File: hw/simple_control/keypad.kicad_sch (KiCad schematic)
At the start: 2 parts, among them U1501 4050

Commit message: chore(hw): add buttons layout
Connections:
- net Filtered Button 4/SW is gone; now on net GND: U1501.11
- net Filtered Button 5/SW is gone; now on net GND: U1501.14
- net BTN4: no longer names the net of U1501.12
- net BTN5: no longer names the net of U1501.15
- no-connect marks 0 -> 2
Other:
- removed sheet Filtered Button 4
- removed sheet Filtered Button 5
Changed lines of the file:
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@@
   (junction (at 204.47 86.36) (diameter 0) (color 0 0 0 0)
   )
+  (no_connect (at 158.75 128.27))
+  (no_connect (at 158.75 116.84))
   (wire (pts (xy 191.77 86.36) (xy 204.47 86.36))
     (stroke (width 0) (type default))
@@
     (stroke (width 0) (type default))
   )
+  (wire (pts (xy 139.7 128.27) (xy 139.7 129.54))
+    (stroke (width 0) (type default))
+  )
   (wire (pts (xy 204.47 86.36) (xy 204.47 90.17))
     (stroke (width 0) (type default))
@@
     (stroke (width 0) (type default))
   )
-  (wire (pts (xy 158.75 128.27) (xy 161.29 128.27))
+  (wire (pts (xy 139.7 116.84) (xy 139.7 118.11))
     (stroke (width 0) (type default))
   )
@@
     (stroke (width 0) (type default))
   )
-  (wire (pts (xy 158.75 116.84) (xy 161.29 116.84))
-    (stroke (width 0) (type default))
-  )
   (wire (pts (xy 204.47 83.82) (xy 204.47 86.36))
     (stroke (width 0) (type default))
@@
     (stroke (width 0) (type default))
   )
-  (global_label "BTN0" (shape output) (at 161.29 69.85 0) (fields_autoplaced)
+  (hierarchical_label "BTN3" (shape output) (at 161.29 105.41 0) (fields_autoplaced)
     (effects (font (size 1.27 1.27)) (justify left))
-    (property "Intersheetrefs" "${INTERSHEET_REFS}" (at 169.0528 69.85 0)
-      (effects (font (size 1.27 1.27)) (justify left) hide)
-    )
-  )
-  (global_label "BTN3" (shape output) (at 161.29 105.41 0) (fields_autoplaced)
+  )
+  (hierarchical_label "BTN1" (shape output) (at 161.29 82.55 0) (fields_autoplaced)
     (effects (font (size 1.27 1.27)) (justify left))
-    (property "Intersheetrefs" "${INTERSHEET_REFS}" (at 169.0528 105.41 0)
-      (effects (font (size 1.27 1.27)) (justify left) hide)
-    )
-  )
-  (global_label "BTN2" (shape output) (at 161.29 93.98 0) (fields_autoplaced)
+  )
+  (hierarchical_label "BTN2" (shape output) (at 161.29 93.98 0) (fields_autoplaced)
     (effects (font (size 1.27 1.27)) (justify left))
-    (property "Intersheetrefs" "${INTERSHEET_REFS}" (at 169.0528 93.98 0)
-      (effects (font (size 1.27 1.27)) (justify left) hide)
-    )
-  )
-  (global_label "BTN4" (shape output) (at 161.29 116.84 0) (fields_autoplaced)
+  )
+  (hierarchical_label "BTN0" (shape output) (at 161.29 69.85 0) (fields_autoplaced)
     (effects (font (size 1.27 1.27)) (justify left))
-    (property "Intersheetrefs" "${INTERSHEET_REFS}" (at 169.0528 116.84 0)
-      (effects (font (size 1.27 1.27)) (justify left) hide)
-    )
-  )
-  (global_label "BTN1" (shape output) (at 161.29 82.55 0) (fields_autoplaced)
-    (effects (font (size 1.27 1.27)) (justify left))
-    (property "Intersheetrefs" "${INTERSHEET_REFS}" (at 169.0528 82.55 0)
-      (effects (font (size 1.27 1.27)) (justify left) hide)
-    )
-  )
-  (global_label "BTN5" (shape output) (at 161.29 128.27 0) (fields_autoplaced)
-    (effects (font (size 1.27 1.27)) (justify left))
-    (property "Intersheetrefs" "${INTERSHEET_REFS}" (at 169.0528 128.27 0)
-      (effects (font (size 1.27 1.27)) (justify left) hide)
-    )
   )
   (symbol (lib_id "4xxx:4050") (at 151.13 93.98 0) (unit 3)
@@
     )
   )
+  (symbol (lib_id "power:GND") (at 139.7 118.11 0) (unit 1)
+    (in_bom yes) (on_board yes) (dnp no) (fields_autoplaced)
+    (property "Reference" "#PWR01501" (at 139.7 124.46 0)
+      (effects (font (size 1.27 1.27)) hide)
+    )
+    (property "Value" "GND" (at 139.7 123.19 0)
+      (effects (font (size 1.27 1.27)))
+    )
+    (property "Footprint" "" (at 139.7 118.11 0)
+      (effects (font (size 1.27 1.27)) hide)
+    )
+    (property "Datasheet" "" (at 139.7 118.11 0)
+      (effects (font (size 1.27 1.27)) hide)
+    )
+    (pin "1")
+    (instances
+      (project "simple_control"
+        (path "/063164e8-0d2a-492b-8a61-e4fa4fbf06a6/3d4e7106-28aa-4335-9fa1-cc7761972854/f10519f0-65c0-40be-a406-8aa448defcff"
+          (reference "#PWR01501") (unit 1)
+        )
+      )
+    )
+  )
+  (symbol (lib_id "power:GND") (at 139.7 129.54 0) (unit 1)
+    (in_bom yes) (on_board yes) (dnp no) (fields_autoplaced)
+    (property "Reference" "#PWR01505" (at 139.7 135.89 0)
+      (effects (font (size 1.27 1.27)) hide)
+    )
+    (property "Value" "GND" (at 139.7 134.62 0)
+      (effects (font (size 1.27 1.27)))
+    )
+    (property "Footprint" "" (at 139.7 129.54 0)
+      (effects (font (size 1.27 1.27)) hide)
+    )
+    (property "Datasheet" "" (at 139.7 129.54 0)
+      (effects (font (size 1.27 1.27)) hide)
+    )
+    (pin "1")
+    (instances
+      (project "simple_control"
+        (path "/063164e8-0d2a-492b-8a61-e4fa4fbf06a6/3d4e7106-28aa-4335-9fa1-cc7761972854/f10519f0-65c0-40be-a406-8aa448defcff"
+          (reference "#PWR01505") (unit 1)
+        )
+      )
+    )
+  )
   (symbol (lib_id "power:+3.3V") (at 204.47 83.82 0) (unit 1)
     (in_bom yes) (on_board yes) (dnp no) (fields_autoplaced)
@@
           (reference "#PWR01502") (unit 1)
         )
+      )
+    )
+  )
+  (sheet (at 111.76 102.87) (size 27.94 5.08) (fields_autoplaced)
+    (stroke (width 0.1524) (type solid))
+    (fill (color 0 0 0 0.0000))
+    (property "Sheetname" "Filtered Button 3" (at 111.76 102.1584 0)
+      (effects (font (size 1.27 1.27)) (justify left bottom))
+    )
+    (property "Sheetfile" "filtered_button.kicad_sch" (at 111.76 108.5346 0)
+      (effects (font (size 1.27 1.27)) (justify left top))
+    )
+    (pin "SW" output (at 139.7 105.41 0)
+      (effects (font (size 1.27 1.27)) (justify right))
+    )
+    (instances
+      (project "simple_control"
+        (path "/063164e8-0d2a-492b-8a61-e4fa4fbf06a6/3d4e7106-28aa-4335-9fa1-cc7761972854" (page "14"))
+        (path "/063164e8-0d2a-492b-8a61-e4fa4fbf06a6/3d4e7106-28aa-4335-9fa1-cc7761972854/f10519f0-65c0-40be-a406-8aa448defcff" (page "20"))
       )
     )
@@
       (project "simple_control"
         (path "/063164e8-0d2a-492b-8a61-e4fa4fbf06a6/3d4e7106-28aa-4335-9fa1-cc7761972854" (page "14"))
-        (path "/063164e8-0d2a-492b-8a61-e4fa4fbf06a6/3d4e7106-28aa-4335-9fa1-cc7761972854/f10519f0-65c0-40be-a406-8aa448defcff" (page "7"))
-      )
-    )
-  )
-  (sheet (at 111.76 125.73) (size 27.94 5.08) (fields_autoplaced)
+        (path "/063164e8-0d2a-492b-8a61-e4fa4fbf06a6/3d4e7106-28aa-4335-9fa1-cc7761972854/f10519f0-65c0-40be-a406-8aa448defcff" (page "18"))
+      )
+    )
+  )
+  (sheet (at 111.76 67.31) (size 27.94 5.08) (fields_autoplaced)
     (stroke (width 0.1524) (type solid))
     (fill (color 0 0 0 0.0000))
-    (property "Sheetname" "Filtered Button 5" (at 111.76 125.0184 0)
+    (property "Sheetname" "Filtered Button 0" (at 111.76 66.5984 0)
       (effects (font (size 1.27 1.27)) (justify left bottom))
     )
-    (property "Sheetfile" "filtered_button.kicad_sch" (at 111.76 131.3946 0)
+    (property "Sheetfile" "filtered_button.kicad_sch" (at 111.76 72.9746 0)
       (effects (font (size 1.27 1.27)) (justify left top))
     )
-    (pin "SW" output (at 139.7 128.27 0)
-      (effects (font (size 1.27 1.27)) (justify right))
-    )
-    (instances
-      (project "simple_control"
-        (path "/063164e8-0d2a-492b-8a61-e4fa4fbf06a6/3d4e7106-28aa-4335-9fa1-cc7761972854" (page "14"))
-        (path "/063164e8-0d2a-492b-8a61-e4fa4fbf06a6/3d4e7106-28aa-4335-9fa1-cc7761972854/f10519f0-65c0-40be-a406-8aa448defcff" (page "19"))
-      )
-    )
-  )
-  (sheet (at 111.76 114.3) (size 27.94 5.08) (fields_autoplaced)
-    (stroke (width 0.1524) (type solid))
-    (fill (color 0 0 0 0.0000))
-    (property "Sheetname" "Filtered Button 4" (at 111.76 113.5884 0)
-      (effects (font (size 1.27 1.27)) (justify left bottom))
-    )
-    (property "Sheetfile" "filtered_button.kicad_sch" (at 111.76 119.9646 0)
-      (effects (font (size 1.27 1.27)) (justify left top))
-    )
-    (pin "SW" output (at 139.7 116.84 0)
-      (effects (font (size 1.27 1.27)) (justify right))
-    )
-    (instances
-      (project "simple_control"
-        (path "/063164e8-0d2a-492b-8a61-e4fa4fbf06a6/3d4e7106-28aa-4335-9fa1-cc7761972854" (page "14"))
-        (path "/063164e8-0d2a-492b-8a61-e4fa4fbf06a6/3d4e7106-28aa-4335-9fa1-cc7761972854/f10519f0-65c0-40be-a406-8aa448defcff" (page "18"))
-      )
-    )
-  )
-  (sheet (at 111.76 102.87) (size 27.94 5.08) (fields_autoplaced)
-    (stroke (width 0.1524) (type solid))
-    (fill (color 0 0 0 0.0000))
-    (property "Sheetname" "Filtered Button 3" (at 111.76 102.1584 0)
-      (effects (font (size 1.27 1.27)) (justify left bottom))
-    )
-    (property "Sheetfile" "filtered_button.kicad_sch" (at 111.76 108.5346 0)
-      (effects (font (size 1.27 1.27)) (justify left top))
-    )
-    (pin "SW" output (at 139.7 105.41 0)
+    (pin "SW" output (at 139.7 69.85 0)
       (effects (font (size 1.27 1.27)) (justify right))
     )
@@
       (project "simple_control"
         (path "/063164e8-0d2a-492b-8a61-e4fa4fbf06a6/3d4e7106-28aa-4335-9fa1-cc7761972854" (page "14"))
-        (path "/063164e8-0d2a-492b-8a61-e4fa4fbf06a6/3d4e7106-28aa-4335-9fa1-cc7761972854/f10519f0-65c0-40be-a406-8aa448defcff" (page "14"))
-      )
-    )
-  )
-  (sheet (at 111.76 67.31) (size 27.94 5.08) (fields_autoplaced)
-    (stroke (width 0.1524) (type solid))
-    (fill (color 0 0 0 0.0000))
-    (property "Sheetname" "Filtered Button 0" (at 111.76 66.5984 0)
-      (effects (font (size 1.27 1.27)) (justify left bottom))
-    )
-    (property "Sheetfile" "filtered_button.kicad_sch" (at 111.76 72.9746 0)
-      (effects (font (size 1.27 1.27)) (justify left top))
-    )
-    (pin "SW" output (at 139.7 69.85 0)
-      (effects (font (size 1.27 1.27)) (justify right))
-    )
-    (instances
-      (project "simple_control"
-        (path "/063164e8-0d2a-492b-8a61-e4fa4fbf06a6/3d4e7106-28aa-4335-9fa1-cc7761972854" (page "14"))
-        (path "/063164e8-0d2a-492b-8a61-e4fa4fbf06a6/3d4e7106-28aa-4335-9fa1-cc7761972854/f10519f0-65c0-40be-a406-8aa448defcff" (page "6"))
-      )
-    )
+        (path "/063164e8-0d2a-492b-8a61-e4fa4fbf06a6/3d4e7106-28aa-4335-9fa1-cc7761972854/f10519f0-65c0-40be-a406-8aa448defcff" (page "19"))
+      )
+    )

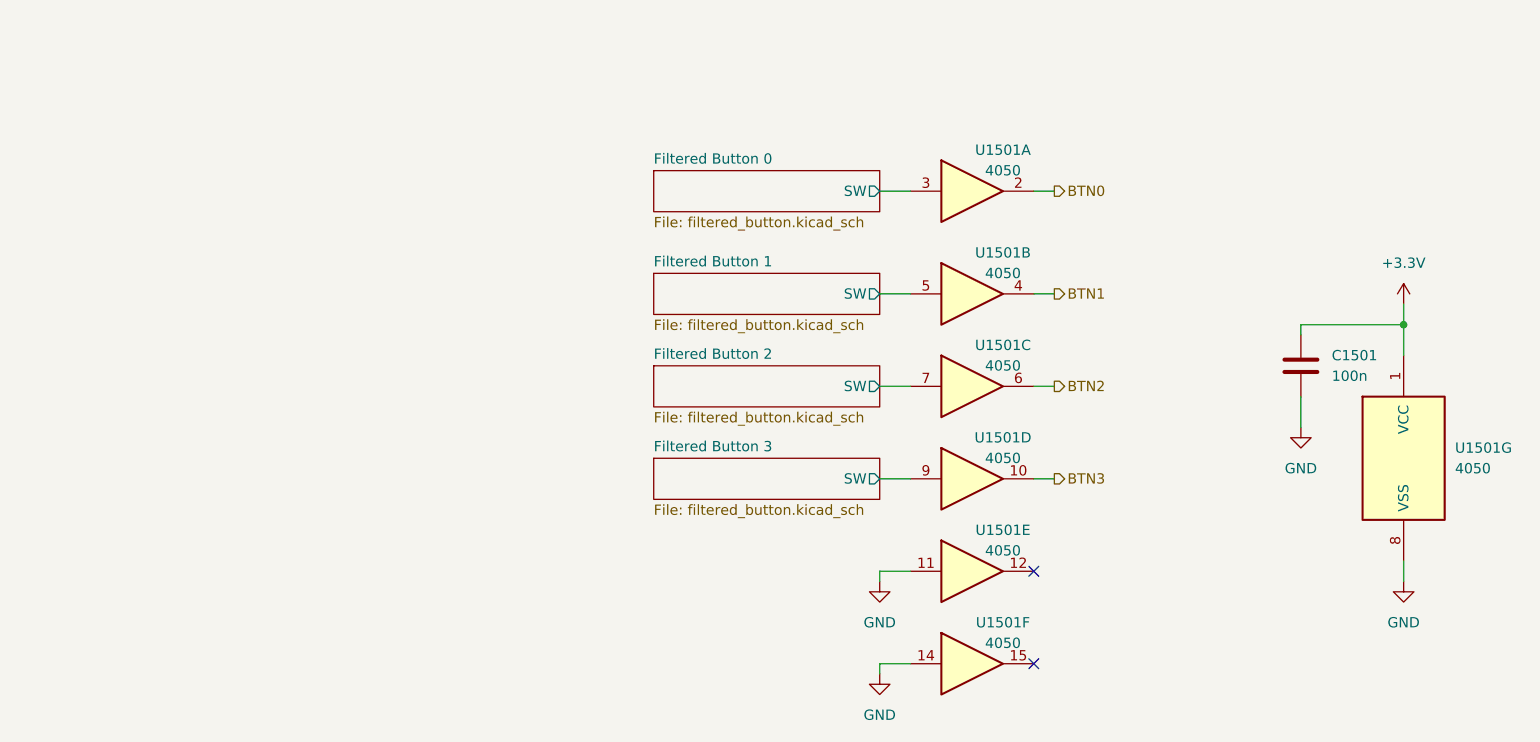
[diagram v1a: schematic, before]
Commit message: chore(hw): switch to 74AHC125 for keypad buffer
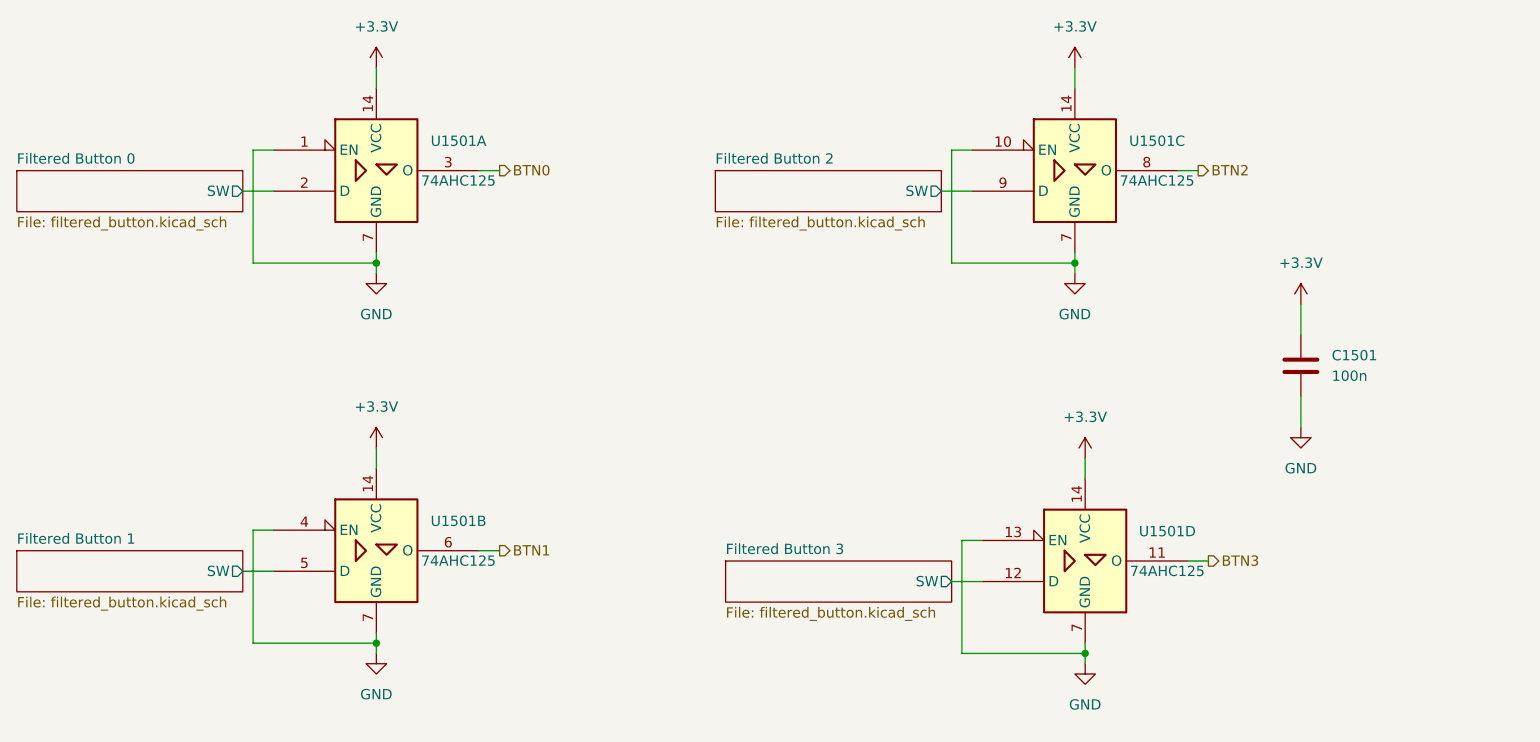
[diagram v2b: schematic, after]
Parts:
- removed U1501: 4050, Package_SO:SO-16_3.9x9.9mm_P1.27mm, symbol 4xxx:4050
- added U1501: 74AHC125, Package_SO:SO-14_3.9x8.65mm_P1.27mm, symbol 74xx_IEEE:74125
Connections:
- net +3.3V: now also U1501.14 (VCC), U1501.14 (VCC), U1501.14 (VCC), U1501.14 (VCC)
- net BTN0: now also U1501.3 (O)
- net BTN1: now also U1501.6 (O)
- net BTN2: now also U1501.8 (O)
- net BTN3: now also U1501.11 (O)
- net Filtered Button 0/SW: now also U1501.2 (D)
- net Filtered Button 1/SW: now also U1501.5 (D)
- net Filtered Button 2/SW: now also U1501.9 (D)
- net Filtered Button 3/SW: now also U1501.12 (D)
- net GND: now also U1501.1 (EN), U1501.10 (EN), U1501.13 (EN), U1501.4 (EN), U1501.7 (GND), U1501.7 (GND), U1501.7 (GND), U1501.7 (GND)
- no-connect marks 2 -> 0
